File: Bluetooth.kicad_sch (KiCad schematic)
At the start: 5 parts

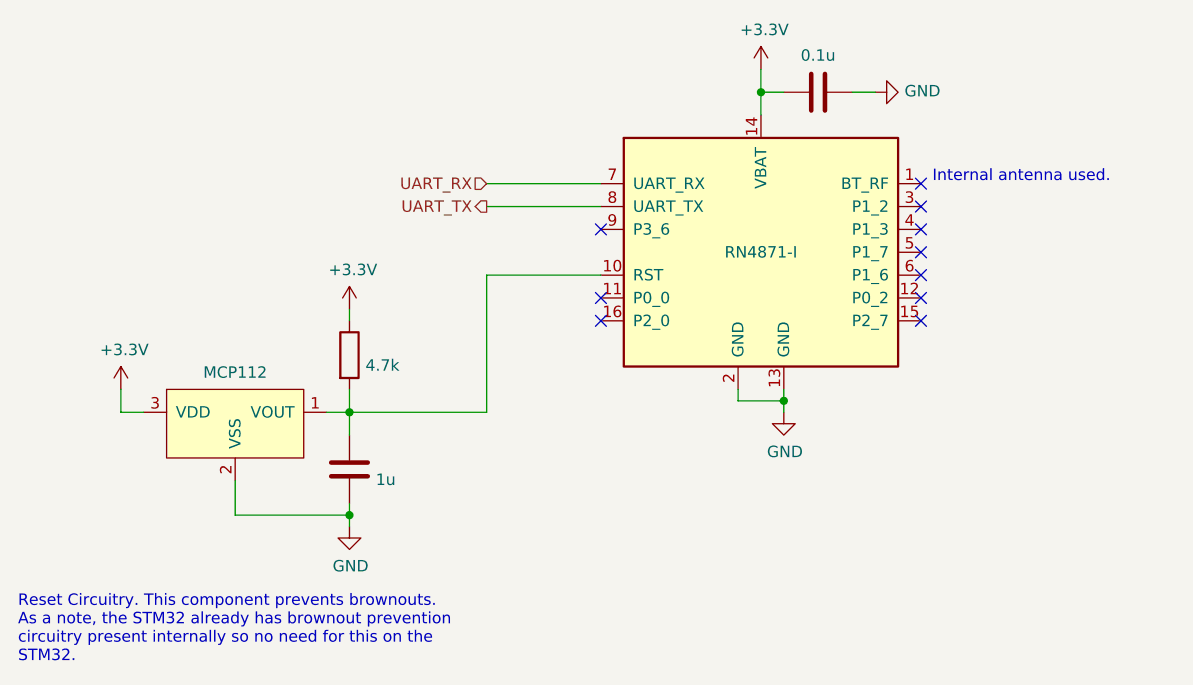
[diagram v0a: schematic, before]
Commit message: Update repo to only use one common library
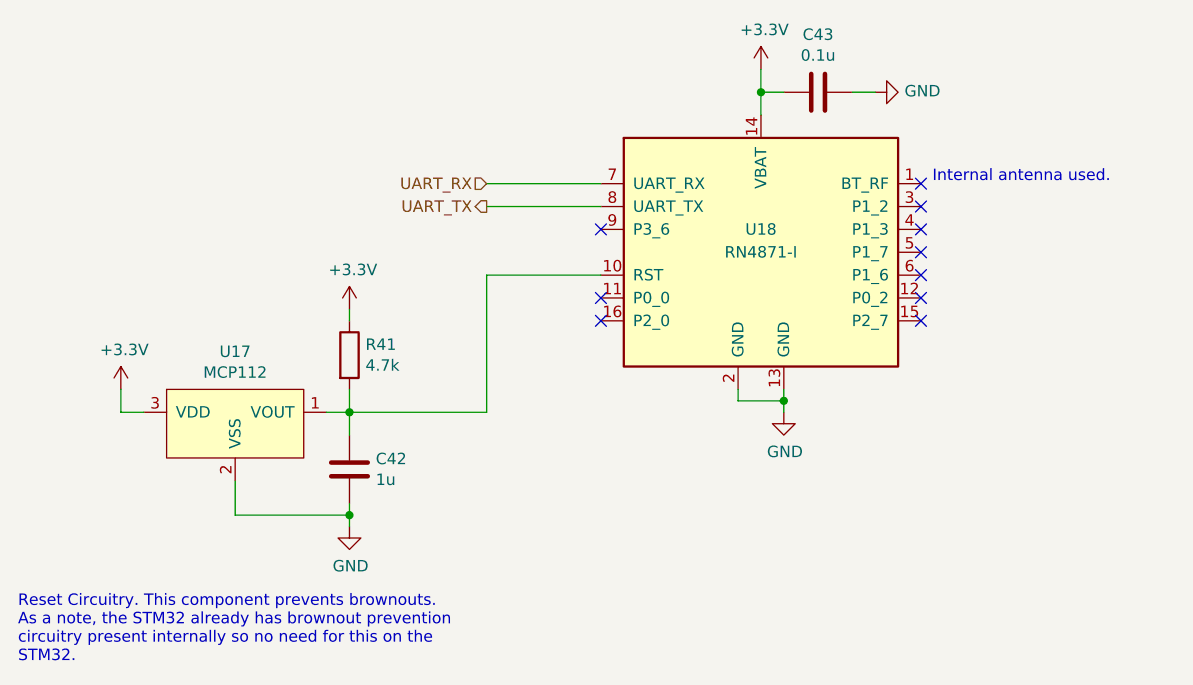
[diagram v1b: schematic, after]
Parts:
- gave numbers to parts that had none: 5
